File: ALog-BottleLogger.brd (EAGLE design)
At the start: 120.7 x 44.5 mm, 109 parts, among them IC2 ATMEGA644M, J6 5.5x2.1mm Barrel, Q10 MOSFET_PCH-IRLML2244, Q11 220mA/50V/3.5Ω, Q12 4.3A/20V/54mΩ, Q13 MOSFET-NCH-BSS138, Q5 4.3A/20V/54mΩ, Q7 4.3A/20V/54mΩ, Q8 220mA/50V/3.5Ω, Q9 220mA/50V/3.5Ω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

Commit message: Updated part data
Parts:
- ADECOUP, C40: device resistor:C0603 -> bschulz_passives:C0603
- C1, C10, C2, C22, C24, C25, C4: device rcl:C0805 -> bschulz_passives:C0805
- C13, C15, C16, C17, C18, C28, C29, C3, C30, C31, C32, C33, C34, C35, C43, C7: device rcl:C0603 -> bschulz_passives:C0603
- D+, D-, R1, R11, R12, R16, R17, R2, R22, R23, R24, R25, R3, R43, R6, R8, R9: device rcl:R0603 -> bschulz_passives:R0603
- IC2: device atmel:MLF44-TH -> bschulz:MLF44-TH
- J1, J14, J15, J16, J2, J8: device SparkFun-Connectors:SCREWTERMINAL-3.5MM-10 -> bschulz:1X10_3.5MM_SCREW
- J4: device SparkFun-Connectors:JST-2-SMD -> bschulz:JST-2-SMD
- MICRO_USB: value 10118194-0001LF_LONGER_PADS -> MICRO_USB_LONGPADS; device 10118194-0001LF:10118194-0001LF_LONGER_PADS -> bschulz:10118194-0001LF_10118194-0001LF_LONGER_PADS
- Q11, Q8, Q9: value 220mA/50V/3.5Ω -> MOSFET-NCH-BSS138; device SparkFun-DiscreteSemi:SOT23-3 -> bschulz:SOT23-3
- Q12, Q5, Q7: value 4.3A/20V/54mΩ -> MOSFET_PCH-IRLML2244; device SparkFun-DiscreteSemi:SOT23-3 -> bschulz:SOT23-3
- R26: device bschulz:R0603 -> bschulz_passives:R0603
- R27: value (none) -> 10k
- RTC1: device SparkFun-Clocks:SO08 -> bschulz:SO08
- R_LED1: device resistor:R0603 -> bschulz_passives:R0603
- S1, U$4: device Custom:SKRPABE010_(SWITCH) -> bschulz:SKRPABE010_(SWITCH)
- U$2: value MAX6070 -> MAX6070AAUT18
- U$3: value TPS62172 -> TPS62172-Q1; device SparkFun-IC-Power:WSON-8-PAD -> bschulz:WSON-8-PAD
- U$7: device linear-technology:QFN38-5X7 -> bschulz:QFN38-5X7
- U2: device FT231X:QFN20 -> bschulz:QFN20
- U3: device microbuilder:PWSON-N10 -> bschulz:PWSON-N10

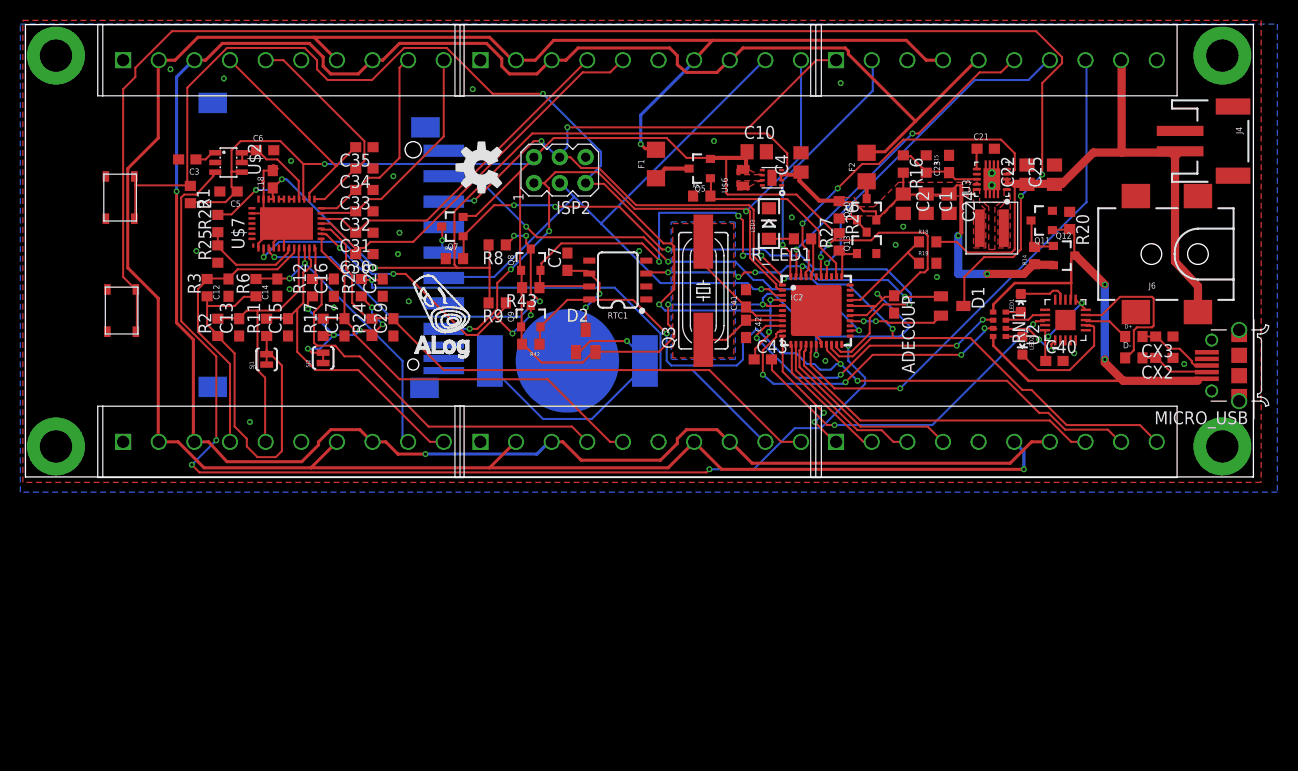
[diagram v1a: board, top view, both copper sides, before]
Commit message: Added comparators, added SCL/SDA connections, updated resistor values and voltage divider sources
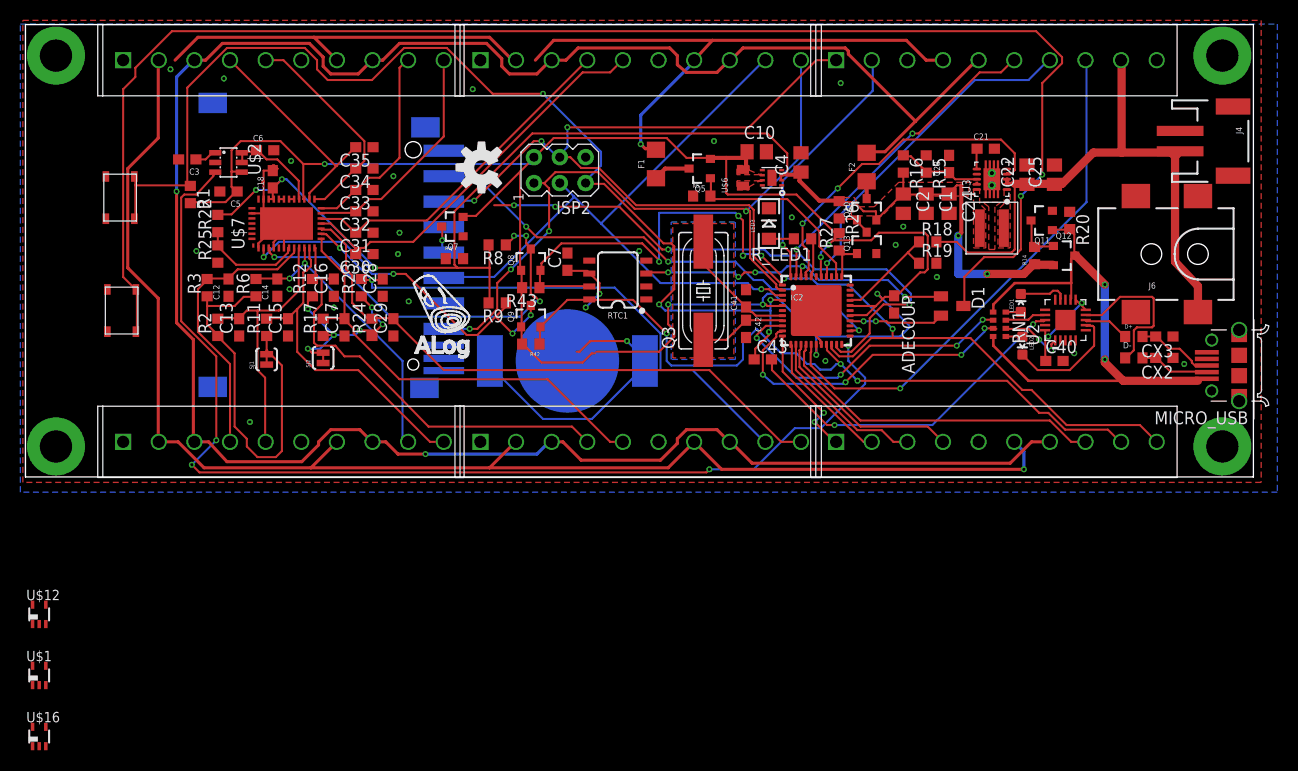
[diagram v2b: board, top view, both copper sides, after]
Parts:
- removed D2: BAT54C, semicon-smd-ipc:SOT23C
- added U$1, U$12, U$16: MIC842, Custom:DCK_R-PDSO-G5
- R15, R19: value 111k -> 180k; device rcl:R0603 -> bschulz_passives:R0603
- R16: value 1M -> 1.62M
- R18: value 1M -> 1.62M; device rcl:R0603 -> bschulz_passives:R0603
- R22, R25: value 10k -> 180k
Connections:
- new net N$14: Q13.1, R27.1, U$1.4
- new net N$19: Q7.1, R4.2, U$16.4
- net +3V3: now also U$1.5, U$12.5, U$16.5; no longer D2.2
- net 3.3V_EXT_CTRL: now also U$12.1; no longer Q5.1, R5.2
- net 5V_EXT_CTRL: now also U$1.1; no longer Q13.1, R27.1
- net EXT_3.3V: now also RTC1.2; no longer J14.P$2, J15.P$2, J16.P$2
- net GND: now also U$1.2, U$12.2, U$16.2; no longer J14.P$1, J15.P$1, J16.P$1, RTC1.2
- net N$37: now also CLOCK_BATT.POWER0, CLOCK_BATT.POWER1; no longer D2.3
- net N$6: now also Q5.1, R5.2, U$12.4; no longer CLOCK_BATT.POWER0, CLOCK_BATT.POWER1, D2.1
- net SCL: now also J14.P$1, J15.P$1, J16.P$1
- net SDA: now also J14.P$2, J15.P$2, J16.P$2
- net SD_VCC_CTRL: now also U$16.1; no longer Q7.1, R4.2
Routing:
- net N$6: track 28.8 -> 0.00 mm, vias 1 -> 0
- net N$37: track 8.88 -> 35.4 mm, vias 2 -> 3
- net SD_VCC_CTRL: track 62.7 -> 56.1 mm
- net EXT_3.3V: track 237.3 -> 233.3 mm
- net 5V_EXT_CTRL: track 4.63 -> 4.01 mm

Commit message: EXT_5V on COM voltage divider on ADC
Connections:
- net +5V: no longer R22.2
- net EXT_5V: now also R22.2
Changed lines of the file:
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@@
 <via x="39.3" y="2.25" extent="1-16" drill="0.3048"/>
 <via x="14.85" y="28.05" extent="1-16" drill="0.3048"/>
+<contactref element="R22" pad="2"/>
+<wire x1="14.85" y1="28.05" x2="18.9" y2="25.75" width="0" layer="19" extent="1-16"/>
 </signal>
 <signal name="ADC6">
@@
 <contactref element="R14" pad="1"/>
 <contactref element="Q12" pad="2"/>
-<contactref element="R22" pad="2"/>
 <contactref element="U$3" pad="3"/>
 <contactref element="U$3" pad="2"/>
@@
 <wire x1="25.2" y1="29.25" x2="24.15" y2="28.2" width="0.2032" layer="16"/>
 <wire x1="24.3" y1="28.35" x2="25.2" y2="29.25" width="0.2032" layer="1"/>
-<wire x1="18.9" y1="25.8" x2="18.9" y2="25.75" width="0.2032" layer="1"/>
 <wire x1="24.3" y1="28.35" x2="24.3" y2="28.4" width="0.2032" layer="1"/>
 <wire x1="45.6" y1="22.8" x2="45.6" y2="20.55" width="0.2032" layer="1"/>
@@
 <vertex x="93.6" y="28.95"/>
 </polygon>
+<wire x1="91.95" y1="28.65" x2="93.475" y2="28.75" width="0" layer="19" extent="1-1"/>
 </signal>
 <signal name="N$40">

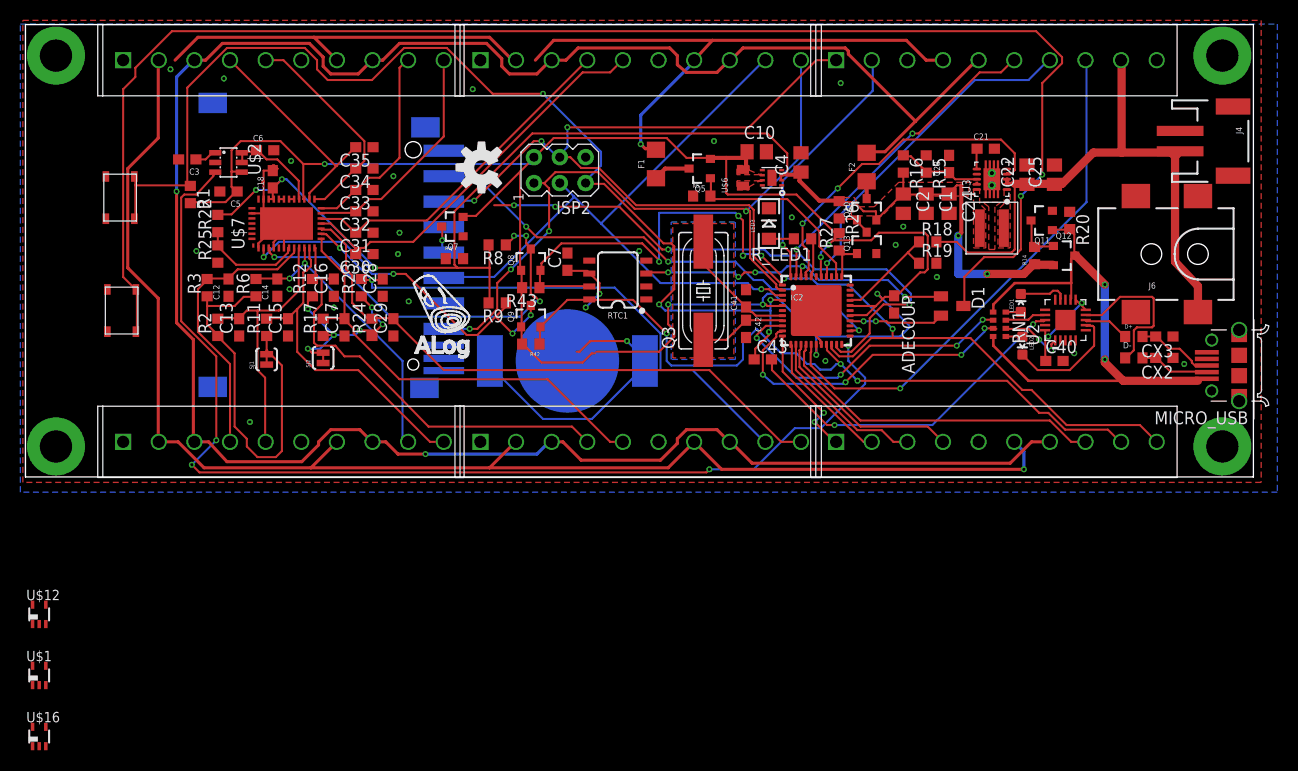
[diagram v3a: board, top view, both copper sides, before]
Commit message: Add comparators for power control, change header layout adding more I2C, change clock power supply
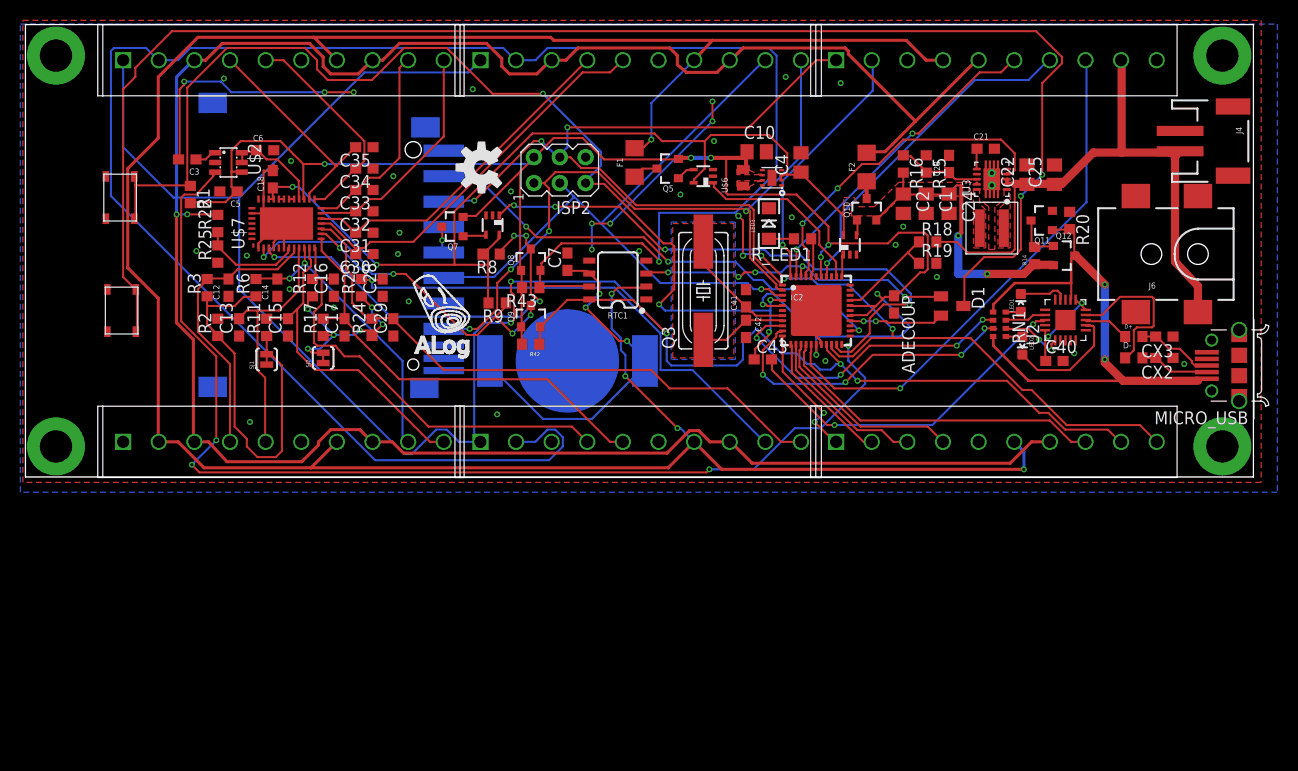
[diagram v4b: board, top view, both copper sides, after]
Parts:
- removed Q13: MOSFET-NCH-BSS138, bschulz:SOT23-3
- removed R26: 10k, bschulz_passives:R0603
- removed R27: 10k, bschulz:R0603
- removed R4, R5: 10k, rcl:R0603
- moved U$1 90.2 mm to (81.0, 22.8)
- moved U$12 78.2 mm to (66.6, 29.6), turned to 90 degrees
- moved U$16 67.2 mm to (45.9, 24.8), turned to 180 degrees
- moved Q5 3.15 mm to (63.1, 30.3)
- moved F1 2.11 mm to (59.9, 30.9)
- moved R8 1.08 mm to (45.8, 21.9)
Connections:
- removed net N$23: Q10.1, Q13.3, R26.2
- net +3V3: no longer R27.2, U$1.5, U$12.5, U$16.5
- net +5V: now also U$1.5, U$12.5, U$16.5; no longer R26.1
- net EXT_5V: no longer J16.P$3
- net GND: now also J16.P$3; no longer Q13.2, R4.1, R5.1
- net N$14: now also Q10.1; no longer Q13.1, R27.1
- net N$19: no longer R4.2
- net N$6: no longer R5.2
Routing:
- net SDA: track 93.9 -> 255.1 mm
- net SCL: track 74.2 -> 202.8 mm, vias 3 -> 5
- net GND: track 27.5 -> 73.1 mm, vias 22 -> 34
- net +3V3: track 200.9 -> 171.0 mm, vias 7 -> 8
- net EXT_3.3V: track 233.3 -> 252.2 mm, vias 2 -> 5
- net +5V: track 129.0 -> 125.4 mm, vias 5 -> 4
- net N$23: track 3.54 -> 0.00 mm
- net EXT_5V: track 229.2 -> 231.5 mm
- net N$19: track 0.00 -> 2.31 mm
- net N$6: track 0.00 -> 1.84 mm
- net 5V_EXT_CTRL: track 4.01 -> 2.23 mm
- net N$14: track 0.00 -> 1.56 mm
- net 3.3V_EXT_CTRL: track 19.1 -> 17.8 mm
- net SDA_HV: track 39.9 -> 41.0 mm
- net N$17: track 3.67 -> 2.56 mm
